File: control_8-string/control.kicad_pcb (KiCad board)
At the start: 2 copper layers, 56 parts, among them J11 CONN_02X04, J12 CONN_01X03, J21 CONN_02X04, J22 CONN_01X03, J3 CONN_01X02, J4 CONN_02X04, J5 CONN_02X04, J6 JACK_2P, J7 DIL_26, U1/2 TL072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

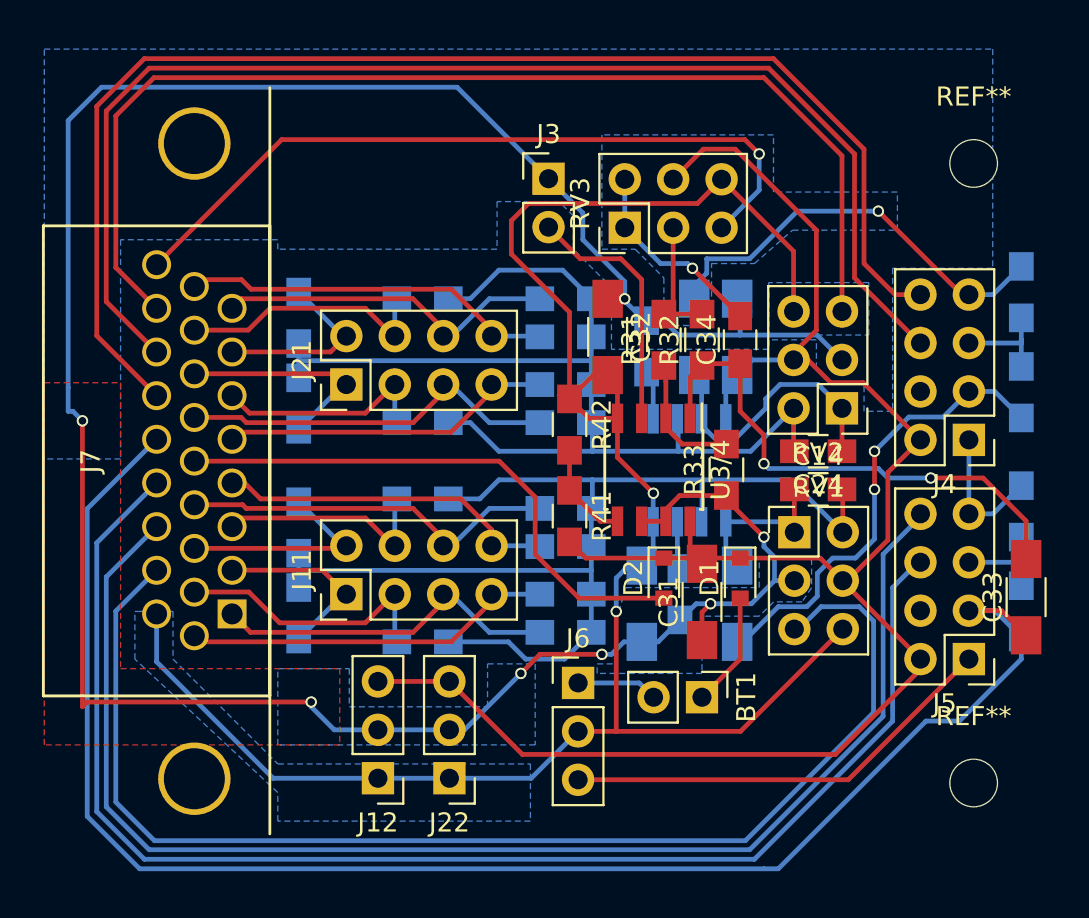
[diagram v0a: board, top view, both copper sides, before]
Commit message: add edge cuts
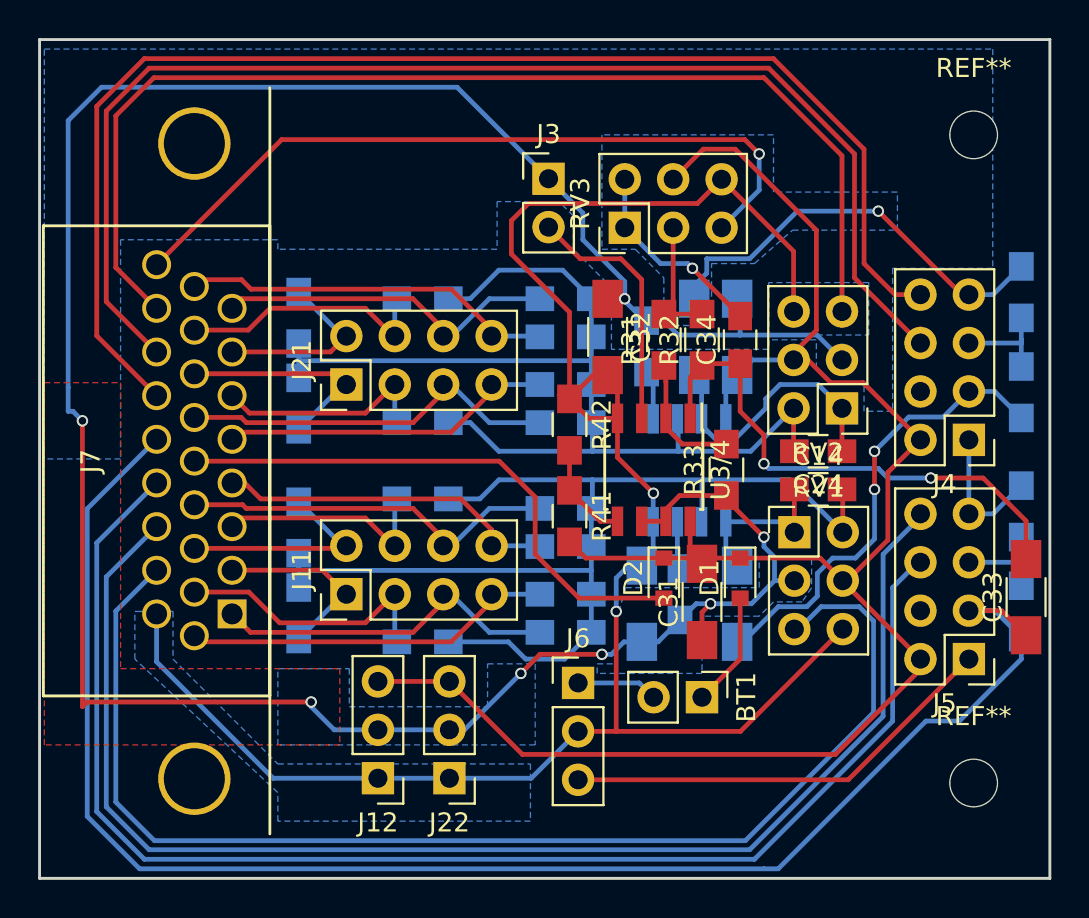
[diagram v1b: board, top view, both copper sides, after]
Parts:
- moved REF** 1.50 mm to (151.9, 91.9)
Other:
- board outline added: 53 x 44 mm
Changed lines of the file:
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@@
     (area 102.830999 86.904 160.034572 131.604001)
     (thickness 1.6)
-    (drawings 1)
+    (drawings 4)
     (tracks 467)
     (zones 0)
@@
   )
   (module Mounting_Holes:MountingHole_2.5mm (layer F.Cu)
-    (at 151.906 93.404)
+    (at 151.906 91.904)
     (descr "Mounting Hole 2.5mm, no annular")
     (tags "mounting hole 2.5mm no annular")
@@
     (pad 1 np_thru_hole circle (at 0 0) (size 2.5 2.5) (drill 2.5) (layers *.Cu *.Mask))
   )
-  (dimension 53 (width 0.3) (layer Margin)
-    (gr_text "53,000 mm" (at 129.406 130.254) (layer Margin)
-      (effects (font (size 1.5 1.5) (thickness 0.3)))
-    )
-    (feature1 (pts (xy 155.906 86.904) (xy 155.906 131.604)))
-    (feature2 (pts (xy 102.906 86.904) (xy 102.906 131.604)))
-    (crossbar (pts (xy 102.906 128.904) (xy 155.906 128.904)))
-    (arrow1a (pts (xy 155.906 128.904) (xy 154.779496 129.490421)))
-    (arrow1b (pts (xy 155.906 128.904) (xy 154.779496 128.317579)))
-    (arrow2a (pts (xy 102.906 128.904) (xy 104.032504 129.490421)))
-    (arrow2b (pts (xy 102.906 128.904) (xy 104.032504 128.317579)))
-  )
+  (gr_line (start 102.906 130.904) (end 102.906 86.904) (angle 90) (layer Edge.Cuts) (width 0.15))
+  (gr_line (start 155.906 130.904) (end 102.906 130.904) (angle 90) (layer Edge.Cuts) (width 0.15))
+  (gr_line (start 155.906 86.904) (end 155.906 130.904) (angle 90) (layer Edge.Cuts) (width 0.15))
+  (gr_line (start 102.906 86.904) (end 155.906 86.904) (angle 90) (layer Edge.Cuts) (width 0.15))
   (segment (start 139.656 116.204) (end 139.656 119.404) (width 0.25) (layer F.Cu) (net 1) (status 10))
   (segment (start 139.656 119.404) (end 137.656 121.404) (width 0.25) (layer F.Cu) (net 1) (status 20))
